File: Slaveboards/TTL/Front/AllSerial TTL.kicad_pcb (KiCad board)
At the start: 2 copper layers, 71.5 x 24 mm, 4 parts

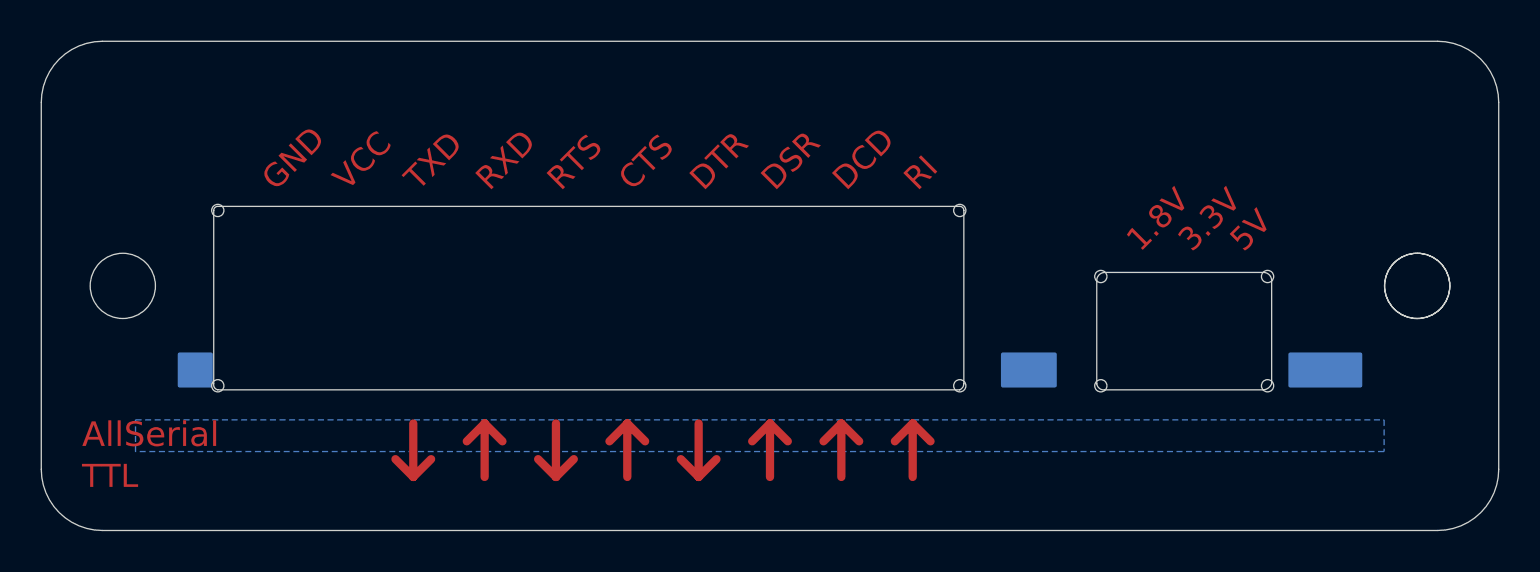
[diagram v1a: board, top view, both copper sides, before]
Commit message: Update AllSerial libraries
update projects
add slave project template
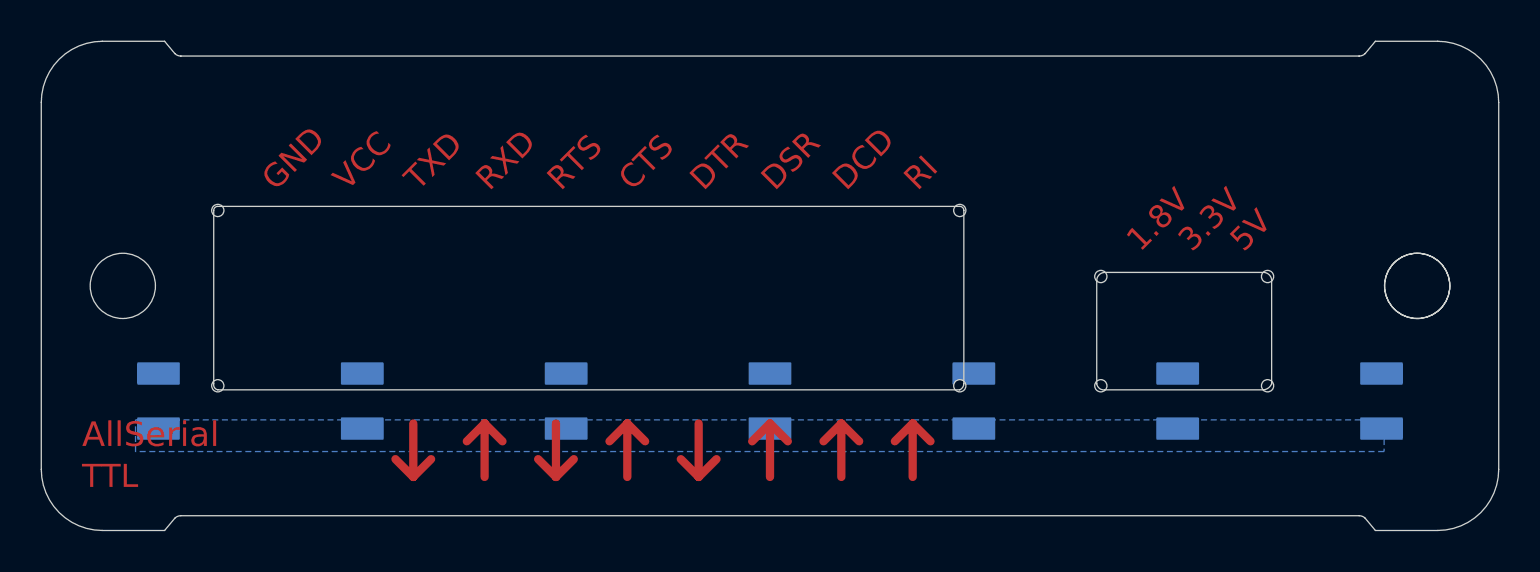
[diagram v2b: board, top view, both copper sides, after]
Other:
- outline, holes or cut-outs redrawn

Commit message: Migrate to KiCad 9
Add eBus board
Add various libraries
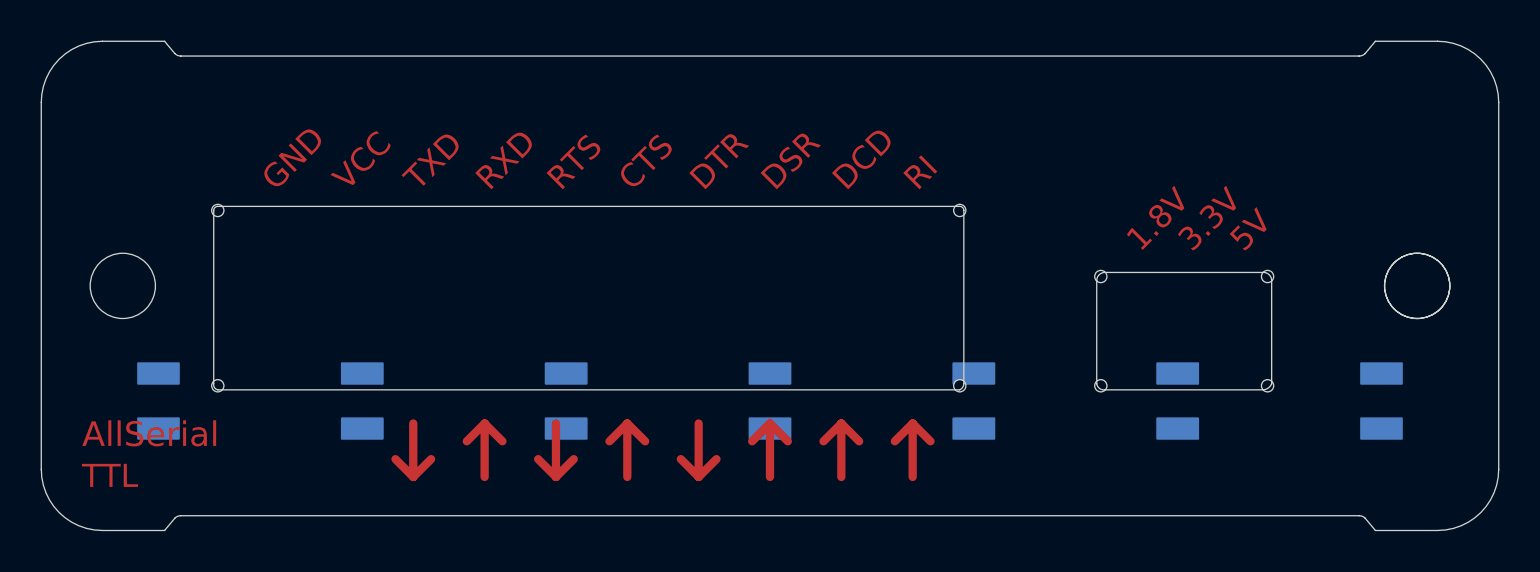
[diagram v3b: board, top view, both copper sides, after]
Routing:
- removed copper zone on B.Cu, net (none)

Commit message: Improve libraries
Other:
- outline, holes or cut-outs redrawn
- board text added: "JLCJLCJLCJLC"

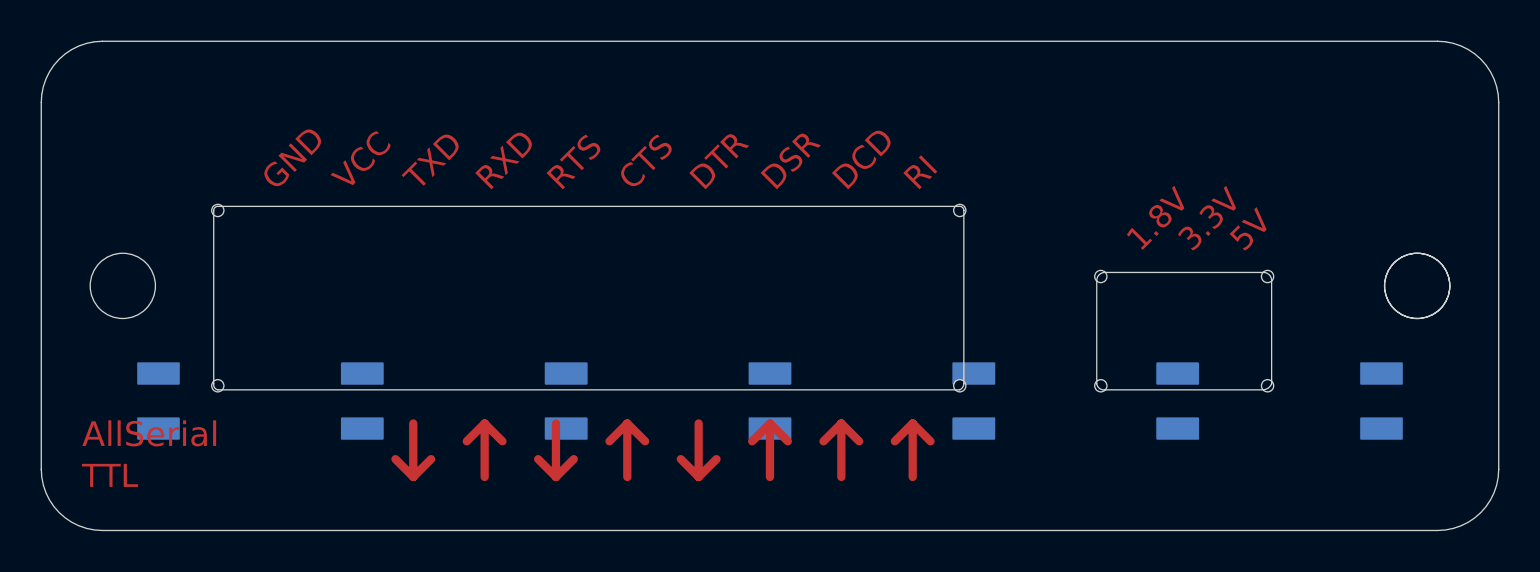
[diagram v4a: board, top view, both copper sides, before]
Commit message: Remove pads from cutouts
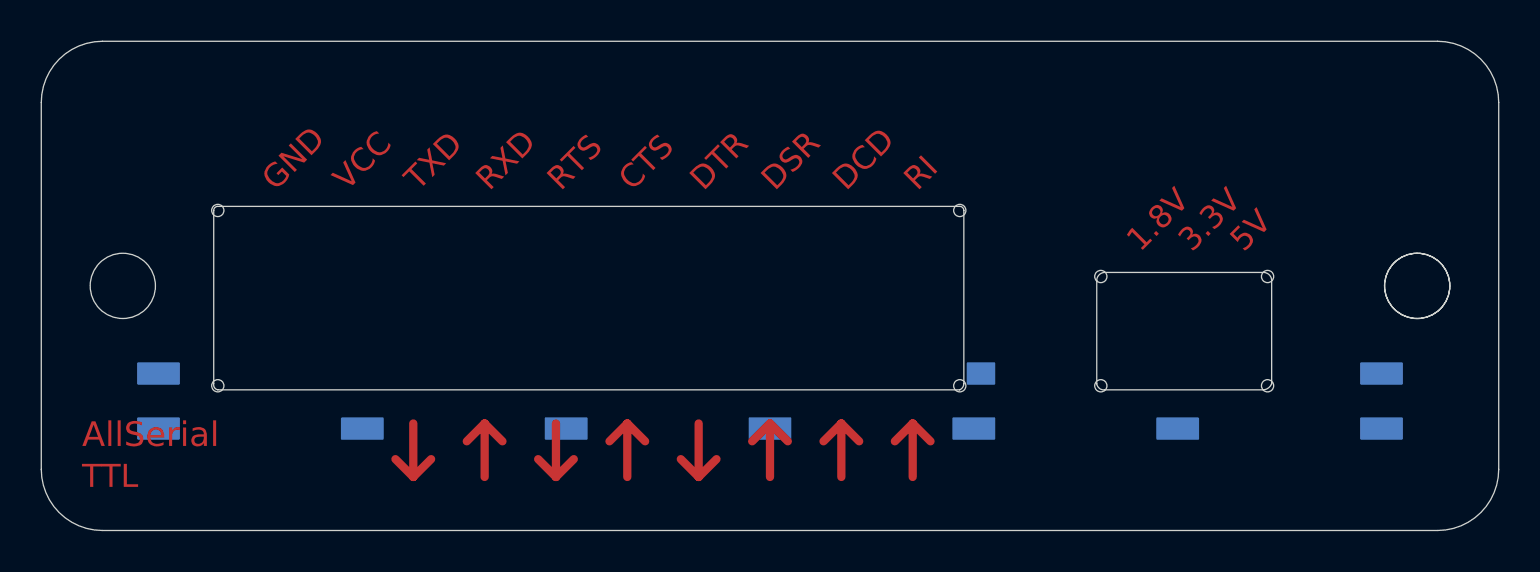
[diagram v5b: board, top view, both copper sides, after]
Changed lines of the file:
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@@
-		)
-		(fp_rect
-			(start -21 -8.2)
-			(end -19 -7.2)
-			(stroke
-				(width 0.1)
-				(type solid)
-			)
-			(fill yes)
-			(layer "B.Cu")
 		)
 		(fp_rect
 			(start -21 -5.5)
 			(end -19 -4.5)
-			(stroke
-				(width 0.1)
-				(type solid)
-			)
-			(fill yes)
-			(layer "B.Cu")
-		)
-		(fp_rect
-			(start -11 -8.2)
-			(end -9 -7.2)
 			(stroke
 				(width 0.1)
@@
 		)
 		(fp_rect
-			(start -1 -8.2)
-			(end 1 -7.2)
-			(stroke
-				(width 0.1)
-				(type solid)
-			)
-			(fill yes)
-			(layer "B.Cu")
-		)
-		(fp_rect
 			(start -1 -5.5)
 			(end 1 -4.5)
-			(stroke
-				(width 0.1)
-				(type solid)
-			)
-			(fill yes)
-			(layer "B.Cu")
-		)
-		(fp_rect
-			(start 9 -8.2)
-			(end 11 -7.2)
 			(stroke
 				(width 0.1)
@@
 		)
 		(fp_rect
-			(start 19 -8.2)
-			(end 21 -7.2)
+			(start 9.7 -8.2)
+			(end 11 -7.2)
 			(stroke
 				(width 0.1)
@@
 		)
 		(fp_rect
-			(start -21 -8.2)
+			(start -21 -5.55)
 			(end -19 -4.5)
 			(stroke
@@
 		)
 		(fp_rect
-			(start -11 -8.2)
+			(start -11 -5.55)
 			(end -9 -4.5)
 			(stroke
@@
 		)
 		(fp_rect
-			(start -1 -8.2)
+			(start -1 -5.55)
 			(end 1 -4.5)
 			(stroke
@@
 		)
 		(fp_rect
-			(start 9 -8.2)
+			(start 9 -5.55)
 			(end 11 -4.5)
 			(stroke
@@
 		)
 		(fp_rect
-			(start 19 -8.2)
+			(start 9.7 -8.2)
+			(end 11 -6.8)
+			(stroke
+				(width 0.1)
+				(type solid)
+			)
+			(fill yes)
+			(layer "B.Mask")
+		)
+		(fp_rect
+			(start 19 -5.55)
 			(end 21 -4.5)
 			(stroke

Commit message: Add python testskript
Add mainboard tester
Add libraries
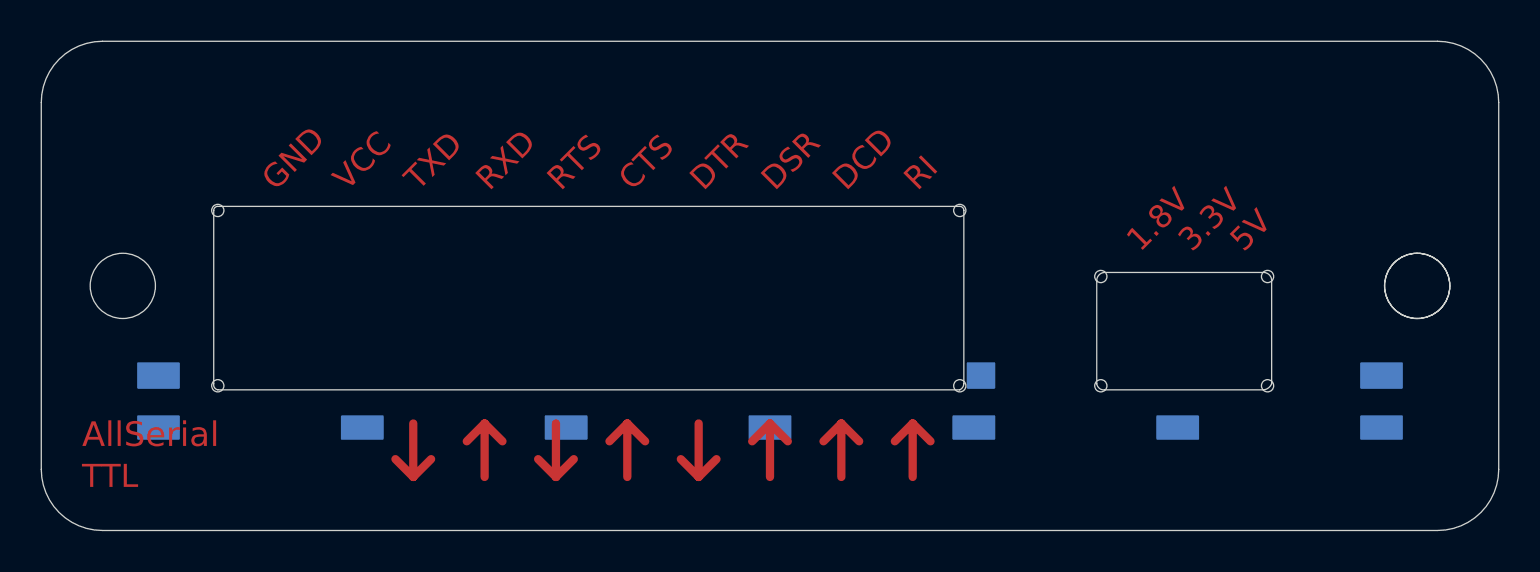
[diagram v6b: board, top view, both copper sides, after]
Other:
- board text added: "AllSerial TTL v1.4 25/23"
- board text removed: "AllSerial TTL front v1.4 25/23"
- board text removed: "JLCJLCJLCJLC"
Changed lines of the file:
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@@
 		(fp_rect
 			(start -31 -8.2)
-			(end -29 -7.2)
+			(end -29 -7)
 			(stroke
 				(width 0.1)
@@
 		)
 		(fp_rect
-			(start -31 -5.5)
+			(start -31 -5.6)
 			(end -29 -4.5)
 			(stroke
@@
 		)
 		(fp_rect
-			(start -21 -5.5)
+			(start -21 -5.6)
 			(end -19 -4.5)
 			(stroke
@@
 		)
 		(fp_rect
-			(start -11 -5.5)
+			(start -11 -5.6)
 			(end -9 -4.5)
 			(stroke
@@
 		)
 		(fp_rect
-			(start -1 -5.5)
+			(start -1 -5.6)
 			(end 1 -4.5)
 			(stroke
@@
 		)
 		(fp_rect
-			(start 9 -5.5)
+			(start 9 -5.6)
 			(end 11 -4.5)
 			(stroke
@@
 		(fp_rect
 			(start 9.7 -8.2)
-			(end 11 -7.2)
+			(end 11 -7)
 			(stroke
 				(width 0.1)
@@
 		)
 		(fp_rect
-			(start 19 -5.5)
+			(start 19 -5.6)
 			(end 21 -4.5)
 			(stroke
@@
 		(fp_rect
 			(start 29 -8.2)
-			(end 31 -7.2)
+			(end 31 -7)
 			(stroke
 				(width 0.1)
@@
 		)
 		(fp_rect
-			(start 29 -5.5)
+			(start 29 -5.6)
 			(end 31 -4.5)
 			(stroke
@@
 		)
 		(fp_rect
-			(start -21 -5.55)
+			(start -21 -8.2)
 			(end -19 -4.5)
 			(stroke
@@
 		)
 		(fp_rect
-			(start -11 -5.55)
+			(start -11 -8.2)
 			(end -9 -4.5)
 			(stroke
@@
 		)
 		(fp_rect
-			(start -1 -5.55)
+			(start -1 -8.2)
 			(end 1 -4.5)
 			(stroke
@@
 		)
 		(fp_rect
-			(start 9 -5.55)
+			(start 9 -8.2)
 			(end 11 -4.5)
 			(stroke
@@
 		)
 		(fp_rect
-			(start 9.7 -8.2)
-			(end 11 -6.8)
-			(stroke
-				(width 0.1)
-				(type solid)
-			)
-			(fill yes)
-			(layer "B.Mask")
-		)
-		(fp_rect
-			(start 19 -5.55)
+			(start 19 -8.2)
 			(end 21 -4.5)
 			(stroke
@@
 		)
 	)
-	(gr_text "AllSerial TTL front v1.4 25/23"
-		(at 168.5011 97.0036 0)
+	(gr_text "AllSerial TTL v1.4 25/23"
+		(at 148.5011 98.4036 0)
 		(layer "B.SilkS")
 		(effects
@@
 				(thickness 0.14224)
 			)
-			(justify left bottom mirror)
-		)
-	)
-	(gr_text "JLCJLCJLCJLC"
-		(at 153.7011 114.7036 0)
-		(layer "B.SilkS")
-		(effects
-			(font
-				(size 1 1)
-				(thickness 0.1)
-			)
-			(justify left bottom mirror)
+			(justify bottom mirror)
 		)
 	)
